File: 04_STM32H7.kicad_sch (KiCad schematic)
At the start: 1 part, among them U3 STM32H743ZIT6

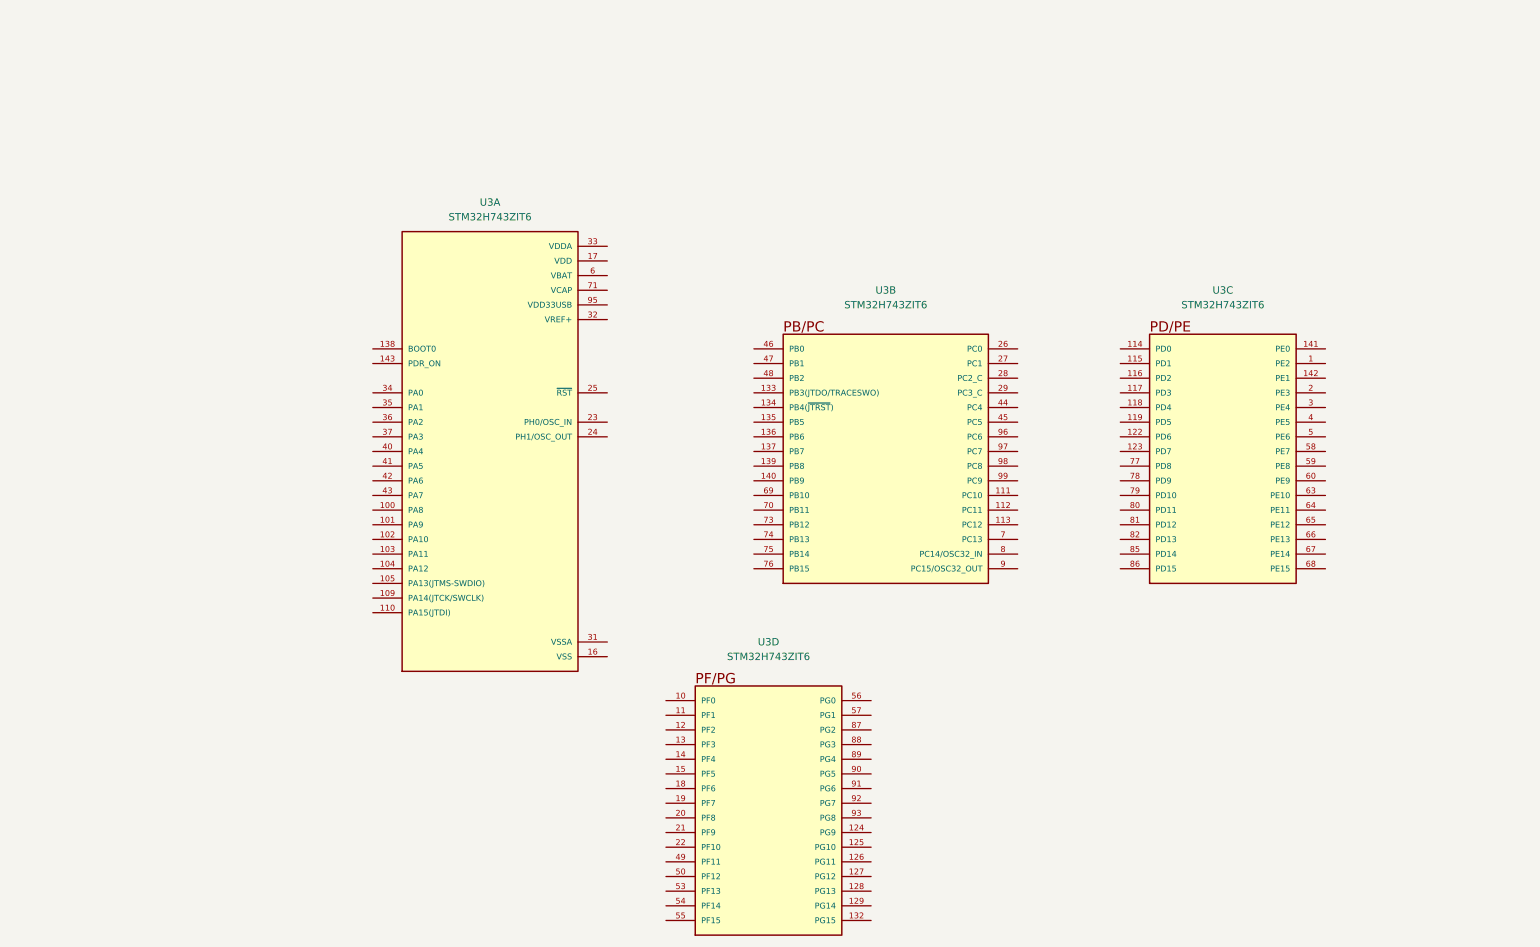
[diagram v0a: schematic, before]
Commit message: connect BNO086 to MCU
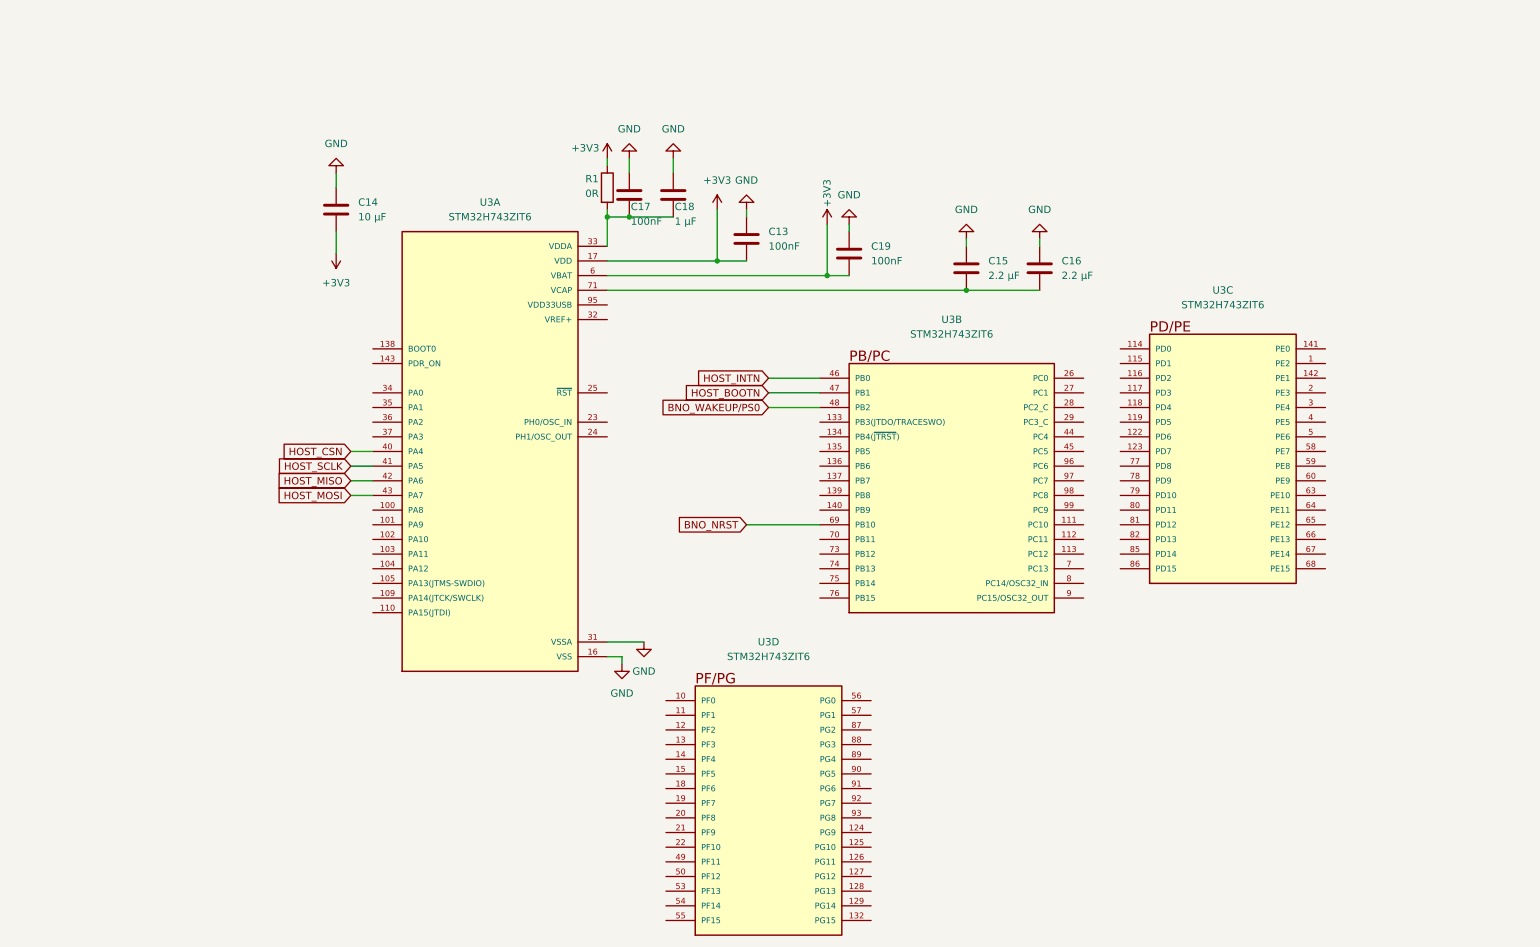
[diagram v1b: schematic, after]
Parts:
- added C13, C17, C19: 100nF, symbol Device:C
- added C14: 10 µF, symbol Device:C
- added C15, C16: 2.2 µF, symbol Device:C
- added C18: 1 µF, symbol Device:C
- added R1: 0R, symbol Device:R
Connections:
- net VDD is gone; now on net +3V3: U3.108 (VDD), U3.121 (VDD), U3.131 (VDD), U3.144 (VDD), U3.17 (VDD), U3.30 (VDD), U3.39 (VDD), U3.52 (VDD), U3.62 (VDD), U3.72 (VDD), U3.84 (VDD)
- net VSS is gone; now on net GND: U3.107 (VSS), U3.120 (VSS), U3.130 (VSS), U3.16 (VSS), U3.38 (VSS), U3.51 (VSS), U3.61 (VSS), U3.83 (VSS), U3.94 (VSS)
- net VCAP: now also C15.2, C16.2
- net GND: now reaches U3.31 (VSSA)
- net GND: now also C13.1, C14.1, C15.1, C16.1, C17.1, C18.1, C19.1
- net at U3.33 (VDDA): now also C17.2, C18.2, R1.2
- net HOST_CSN: now reaches U3.40 (PA4)
- net HOST_SCLK: now reaches U3.41 (PA5)
- net HOST_MISO: now reaches U3.42 (PA6)
- net HOST_MOSI: now reaches U3.43 (PA7)
- net +3V3: now reaches U3.6 (VBAT)
- net +3V3: now also C13.2, C14.2, C19.2, R1.1
- net HOST_INTN: now reaches U3.46 (PB0)
- net HOST_BOOTN: now reaches U3.47 (PB1)
- net BNO_WAKEUP/PS0: now reaches U3.48 (PB2)
- net BNO_NRST: now reaches U3.69 (PB10)
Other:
- moved on the sheet: U3B

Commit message: added footprints R and C and more
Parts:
- C13, C14, C15, C16, C17, C18, C19: footprint (none) -> Capacitor_SMD:C_0805_2012Metric_Pad1.18x1.45mm_HandSolder
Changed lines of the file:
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@@
 			)
 		)
-		(property "Footprint" ""
+		(property "Footprint" "Capacitor_SMD:C_0805_2012Metric_Pad1.18x1.45mm_HandSolder"
 			(at 133.0452 52.07 0)
 			(hide yes)
@@
 			)
 		)
-		(property "Footprint" ""
+		(property "Footprint" "Capacitor_SMD:C_0805_2012Metric_Pad1.18x1.45mm_HandSolder"
 			(at 163.5252 62.23 0)
 			(hide yes)
@@
 			)
 		)
-		(property "Footprint" ""
+		(property "Footprint" "Capacitor_SMD:C_0805_2012Metric_Pad1.18x1.45mm_HandSolder"
 			(at 74.6252 54.61 0)
 			(hide yes)
@@
 			)
 		)
-		(property "Footprint" ""
+		(property "Footprint" "Capacitor_SMD:C_0805_2012Metric_Pad1.18x1.45mm_HandSolder"
 			(at 145.7452 59.69 0)
 			(hide yes)
@@
 			)
 		)
-		(property "Footprint" ""
+		(property "Footprint" "Capacitor_SMD:C_0805_2012Metric_Pad1.18x1.45mm_HandSolder"
 			(at 183.8452 64.77 0)
 			(hide yes)
@@
 			)
 		)
-		(property "Footprint" ""
+		(property "Footprint" "Capacitor_SMD:C_0805_2012Metric_Pad1.18x1.45mm_HandSolder"
 			(at 125.4252 52.07 0)
 			(hide yes)
@@
 			)
 		)
-		(property "Footprint" ""
+		(property "Footprint" "Capacitor_SMD:C_0805_2012Metric_Pad1.18x1.45mm_HandSolder"
 			(at 196.5452 64.77 0)
 			(hide yes)

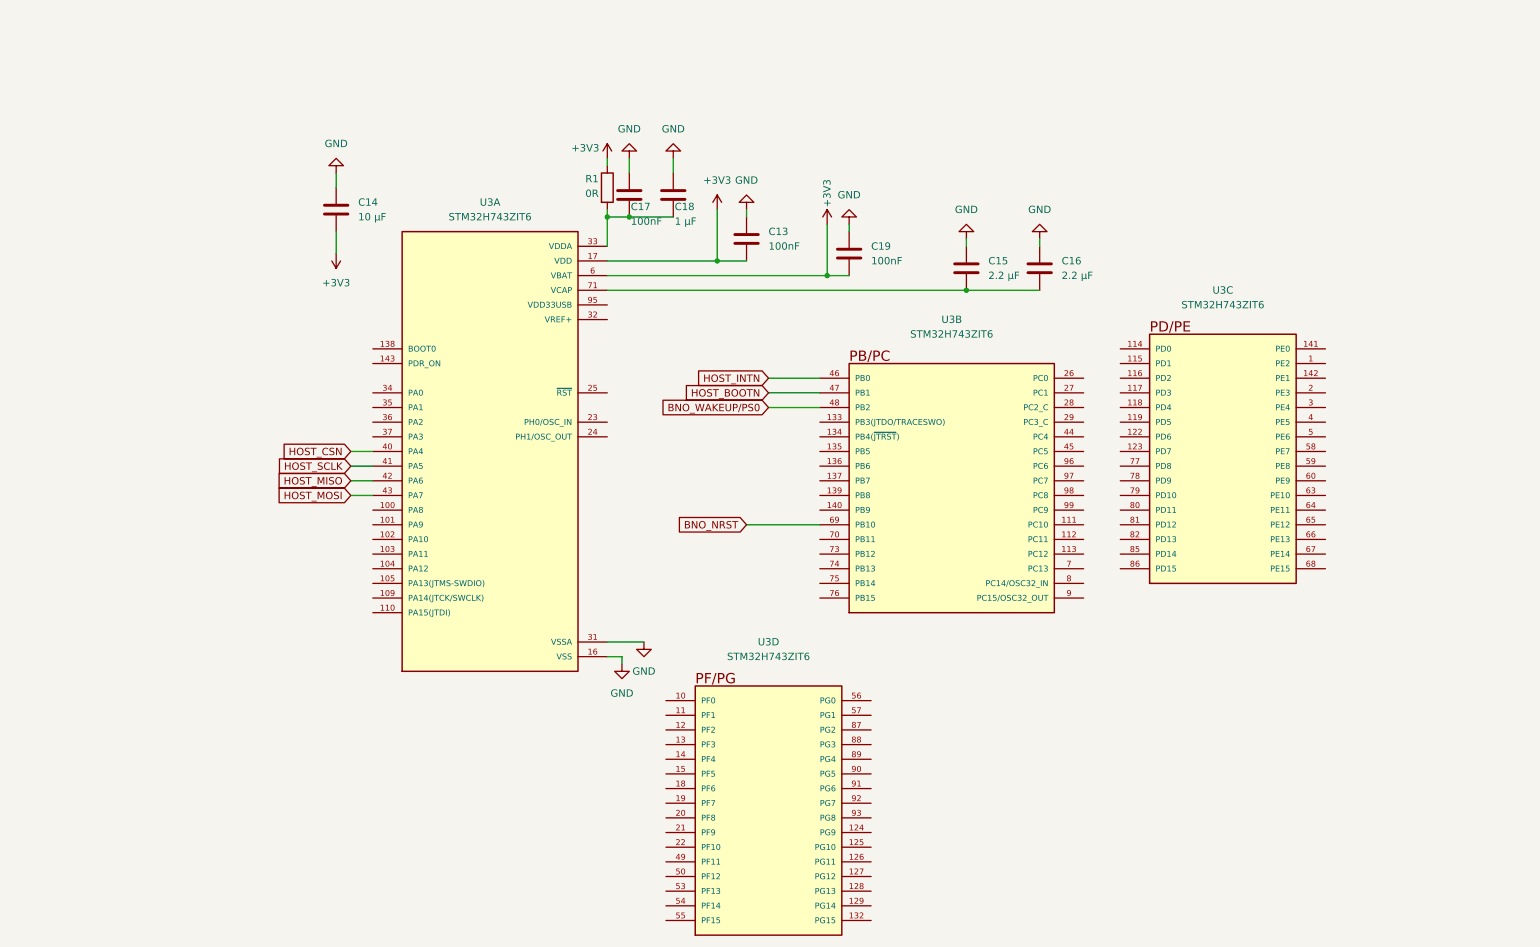
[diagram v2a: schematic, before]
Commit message: added footprints and connect usb33c MCU to power and VREF+ to REF3033
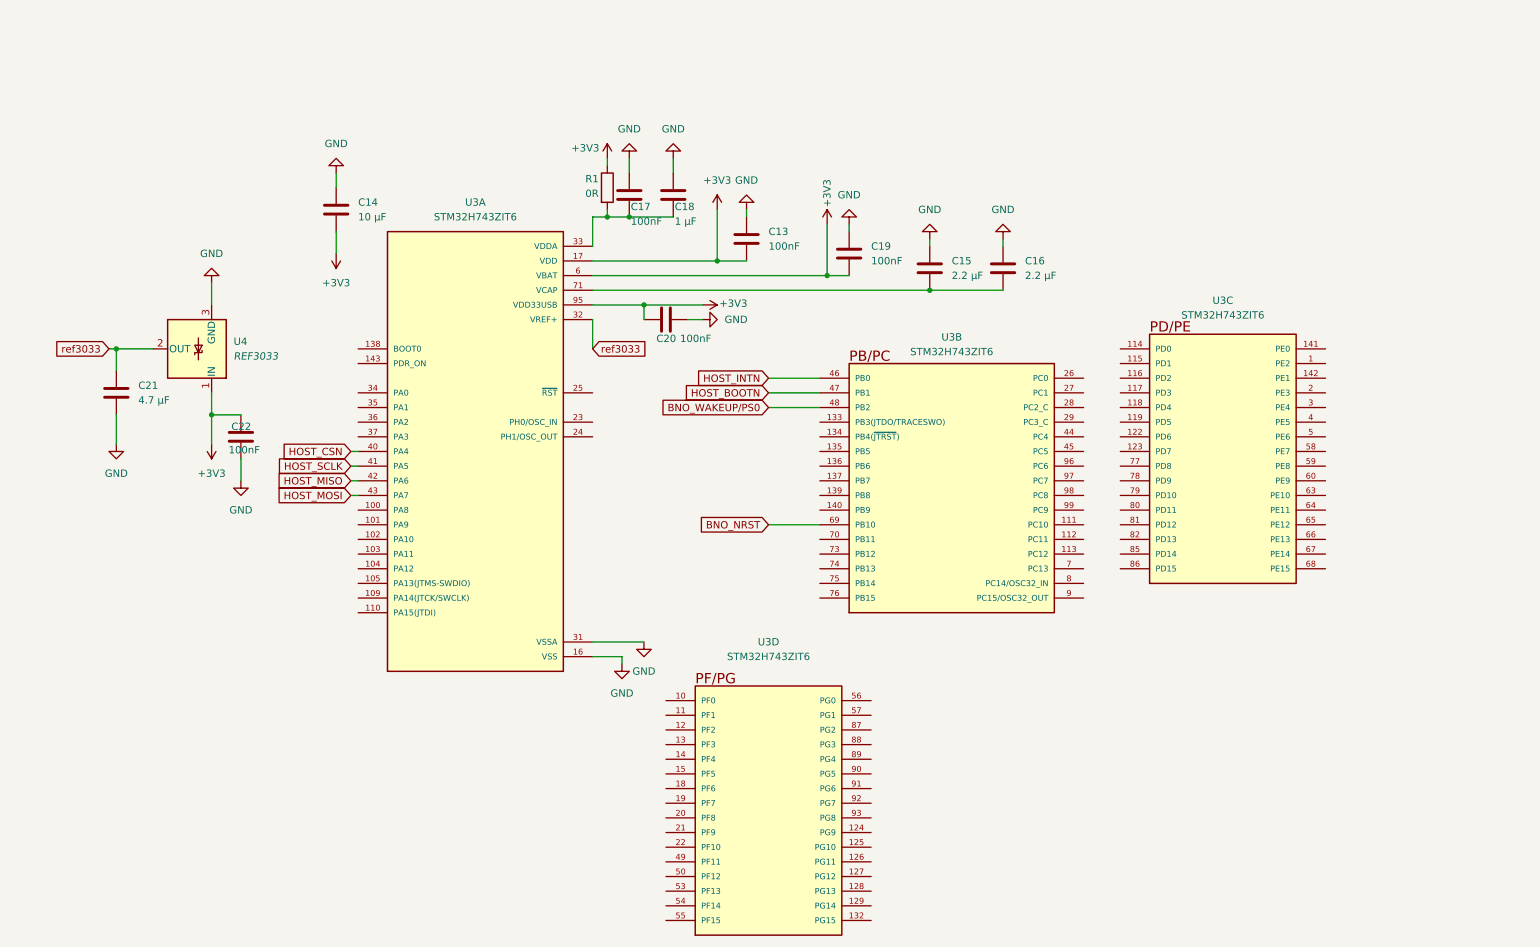
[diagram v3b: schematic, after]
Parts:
- added C20, C22: 100nF, Capacitor_SMD:C_0805_2012Metric_Pad1.18x1.45mm_HandSolder, symbol Device:C
- added C21: 4.7 µF, Capacitor_SMD:C_0805_2012Metric_Pad1.18x1.45mm_HandSolder, symbol Device:C
- added U4: REF3033, Package_TO_SOT_SMD:SOT-23, symbol Reference_Voltage:REF3033
- U3: footprint STM32H743ZIT6:QFP50P2200X2200X160-144N -> STM32H743ZIT6:QFP50P2200X2200X160
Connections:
- net +3V3: now also U3.95 (VDD33USB), C20.1, C22.2, U4.1 (IN)
- net GND: now also C20.2, C21.2, C22.1, U4.3 (GND)
- net ref3033: now reaches U3.32 (VREF+)
- net ref3033: now also C21.1, U4.2 (OUT)
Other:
- moved on the sheet: C15, C16, U3A

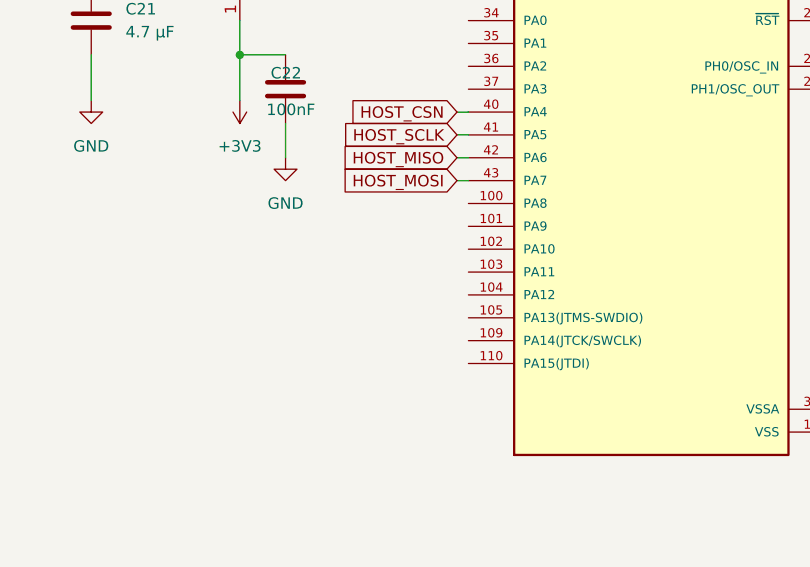
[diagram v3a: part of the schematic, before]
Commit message: added USB-C CDC schem
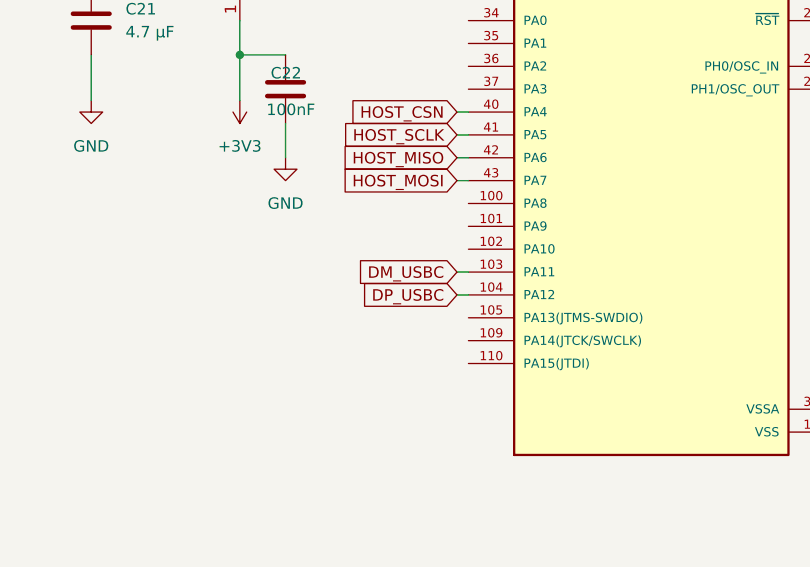
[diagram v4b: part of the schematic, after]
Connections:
- net DM_USBC: now reaches U3.103 (PA11)
- net DP_USBC: now reaches U3.104 (PA12)
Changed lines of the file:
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@@
+	(wire
+		(pts
+			(xy 76.2 113.03) (xy 77.47 113.03)
+		)
+		(stroke
+			(width 0)
+			(type default)
+		)
+	)
 	(wire
 		(pts
@@
 	(wire
 		(pts
+			(xy 76.2 110.49) (xy 77.47 110.49)
+		)
+		(stroke
+			(width 0)
+			(type default)
+		)
+	)
+	(wire
+		(pts
 			(xy 139.7 50.8) (xy 139.7 59.69)
 		)
@@
 		)
 	)
+	(global_label "DP_USBC"
+		(shape input)
+		(at 76.2 113.03 180)
+		(fields_autoplaced yes)
+		(effects
+			(font
+				(size 1.27 1.27)
+			)
+			(justify right)
+		)
+		(property "Intersheetrefs" "${INTERSHEET_REFS}"
+			(at 64.6272 113.03 0)
+			(hide yes)
+			(show_name no)
+			(do_not_autoplace no)
+			(effects
+				(font
+					(size 1.27 1.27)
+				)
+				(justify right)
+			)
+		)
+	)
 	(global_label "BNO_NRST"
 		(shape input)
@@
 			(hide yes)
 			(show_name no)
+			(do_not_autoplace no)
+			(effects
+				(font
+					(size 1.27 1.27)
+				)
+				(justify right)
+			)
+		)
+	)
+	(global_label "DM_USBC"
+		(shape input)
+		(at 76.2 110.49 180)
+		(fields_autoplaced yes)
+		(effects
+			(font
+				(size 1.27 1.27)
+			)
+			(justify right)
+		)
+		(property "Intersheetrefs" "${INTERSHEET_REFS}"
+			(at 64.4458 110.49 0)
+			(hide yes)
+			(show_name no)

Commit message: start place components
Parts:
- R1: value 0R -> R; footprint (none) -> Resistor_SMD:R_0805_2012Metric_Pad1.20x1.40mm_HandSolder
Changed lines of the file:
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@@
+	)
+	(symbol
+		(lib_id "Device:R")
+		(at 120.65 46.99 0)
+		(unit 1)
+		(body_style 1)
+		(exclude_from_sim no)
+		(in_bom yes)
+		(on_board yes)
+		(in_pos_files yes)
+		(dnp no)
+		(property "Reference" "R1"
+			(at 116.84 45.466 0)
+			(show_name no)
+			(do_not_autoplace no)
+			(effects
+				(font
+					(size 1.27 1.27)
+				)
+				(justify left)
+			)
+		)
+		(property "Value" "R"
+			(at 116.84 48.006 0)
+			(show_name no)
+			(do_not_autoplace no)
+			(effects
+				(font
+					(size 1.27 1.27)
+				)
+				(justify left)
+			)
+		)
+		(property "Footprint" "Resistor_SMD:R_0805_2012Metric_Pad1.20x1.40mm_HandSolder"
+			(at 118.872 46.99 90)
+			(hide yes)
+			(show_name no)
+			(do_not_autoplace no)
+			(effects
+				(font
+					(size 1.27 1.27)
+				)
+			)
+		)
+		(property "Datasheet" ""
+			(at 120.65 46.99 0)
+			(hide yes)
+			(show_name no)
+			(do_not_autoplace no)
+			(effects
+				(font
+					(size 1.27 1.27)
+				)
+			)
+		)
+		(property "Description" "Resistor"
+			(at 120.65 46.99 0)
+			(hide yes)
+			(show_name no)
+			(do_not_autoplace no)
+			(effects
+				(font
+					(size 1.27 1.27)
+				)
+			)
+		)
+		(pin "2"
+		)
+		(pin "1"
+		)
+		(instances
+			(project "pesokbot_board"
+				(path "/3b0b46ed-3ce3-4874-97d9-085fc63ec69d/d4987e84-6bd1-43f6-b376-fd16621737cc"
+					(reference "R1")
+					(unit 1)
+				)
+			)
+		)
 	)
 	(symbol
@@
 					(unit 1)
 				)
-			)
-		)
-	)
-	(symbol
-		(lib_id "Device:R")
-		(at 120.65 46.99 0)
-		(unit 1)
-		(body_style 1)
-		(exclude_from_sim no)
-		(in_bom yes)
-		(on_board yes)
-		(in_pos_files yes)
-		(dnp no)
-		(property "Reference" "R1"
-			(at 116.84 45.466 0)
-			(show_name no)
-			(do_not_autoplace no)
-			(effects
-				(font
-					(size 1.27 1.27)
-				)
-				(justify left)
-			)
-		)
-		(property "Value" "0R"
-			(at 116.84 48.006 0)
-			(show_name no)
-			(do_not_autoplace no)
-			(effects
-				(font
-					(size 1.27 1.27)
-				)
-				(justify left)
-			)
-		)
-		(property "Footprint" ""
-			(at 118.872 46.99 90)
-			(hide yes)
-			(show_name no)
-			(do_not_autoplace no)
-			(effects
-				(font
-					(size 1.27 1.27)
-				)
-			)
-		)
-		(property "Datasheet" ""
-			(at 120.65 46.99 0)
-			(hide yes)
-			(show_name no)
-			(do_not_autoplace no)
-			(effects
-				(font
-					(size 1.27 1.27)
-				)
-			)
-		)
-		(property "Description" "Resistor"
-			(at 120.65 46.99 0)
-			(hide yes)
-			(show_name no)
-			(do_not_autoplace no)
-			(effects
-				(font
-					(size 1.27 1.27)
-				)
-			)
-		)
-		(pin "1"
-		)
-		(pin "2"
-		)
-		(instances
-			(project "pesokbot_board"
-				(path "/3b0b46ed-3ce3-4874-97d9-085fc63ec69d/d4987e84-6bd1-43f6-b376-fd16621737cc"
-					(reference "R1")
-					(unit 1)
-				)
